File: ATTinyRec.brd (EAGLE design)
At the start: 15.7 x 29.3 mm, 10 parts, among them IC1 MAX631CPA, IC2 REG1117, M1 ELECTRET_MICROPHON-WM-62PC/62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, U1 ATTINY85-20SU, U2 USD-SOCKETUSD

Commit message: Debugging
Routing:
- net N$10: track 50.1 -> 69.5 mm, vias 0 -> 1
- net N$8: track 9.90 -> 0.00 mm, vias 1 -> 0
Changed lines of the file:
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@@
 <contactref element="M1" pad="1"/>
 <contactref element="R1" pad="2"/>
-<wire x1="14.1732" y1="25.8318" x2="13.716" y2="26.289" width="0.254" layer="1"/>
-<wire x1="16.2306" y1="25.8318" x2="14.1732" y2="25.8318" width="0.254" layer="1"/>
-<wire x1="17.3736" y1="24.6888" x2="16.2306" y2="25.8318" width="0.254" layer="1"/>
-<wire x1="17.3736" y1="24.6888" x2="17.46" y2="24.511" width="0.254" layer="1"/>
-<via x="16.2306" y="25.8318" extent="1-16" drill="0.6"/>
-<wire x1="16.2306" y1="25.8318" x2="18.685" y2="25.8318" width="0.4064" layer="16"/>
-<wire x1="18.685" y1="25.8318" x2="18.685" y2="28.763" width="0.4064" layer="16"/>
+<wire x1="17.46" y1="24.511" x2="18.685" y2="28.763" width="0" layer="19" extent="1-1"/>
 </signal>
 <signal name="N$9">
@@
 <wire x1="9.8298" y1="23.3172" x2="9.8298" y2="24.6888" width="0.254" layer="1"/>
 <wire x1="11.176" y1="21.971" x2="9.8298" y2="23.3172" width="0.254" layer="1"/>
-<wire x1="9.8298" y1="24.6888" x2="17.018" y2="27.1526" width="0" layer="19" extent="1-1"/>
-<wire x1="9.406" y1="24.257" x2="9.8298" y2="24.6888" width="0" layer="19" extent="1-1"/>
+<wire x1="17.018" y1="27.1526" x2="18.796" y2="27.1526" width="0.4064" layer="1"/>
+<wire x1="18.796" y1="27.1526" x2="18.796" y2="26.924" width="0.4064" layer="1"/>
+<via x="18.796" y="26.924" extent="1-16" drill="0.6" shape="square"/>
+<wire x1="18.796" y1="26.924" x2="18.796" y2="19.558" width="0.4064" layer="16"/>
+<wire x1="18.796" y1="19.558" x2="11.176" y2="19.558" width="0.4064" layer="16"/>
+<wire x1="11.176" y1="19.558" x2="11.176" y2="21.971" width="0.4064" layer="16"/>
+<wire x1="9.8298" y1="24.6888" x2="9.406" y2="24.257" width="0" layer="19" extent="1-1"/>
 </signal>
 <signal name="N$11">

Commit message: Component Replacements
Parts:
- removed IC1: MAX631CPA, maxim:DIL08
- removed IC2: REG1117, burr-brown:SOT223
- removed LED1: (no value), led:SMARTLED-TTW
- added C2: 10 µF, rcl:C0805K
- added D1: (no value), diode:DO214AC
- added JP1: AVR_SPI_PRG_6TESTPOINTS, SparkFun-Connectors:2X3_TEST_POINTS
- added R2: 976k, resistor:M0805
- added R3: 562k, resistor:M0805
- added U$1: MCP1640, GeekAmmo:SOT23-6
- C1: value 100 ÂµF -> 4.7 µF
- L1: value (none) -> 4.7 µH
- U1: value ATTINY85-20SU -> (none); device Atmel_By_element14_Batch_1-00:SOIC127P798X216-8N -> SparkFun-DigitalIC:MLF32-PAD
- moved M1 69.4 mm to (-47.0, 47.0)
- moved R1 66.3 mm to (-41.9, 55.9)
- moved C1 63.2 mm to (-48.3, 54.6), turned to 0 degrees
- moved U2 57.0 mm to (-21.6, 6.35), turned to 0 degrees
- moved L1 48.0 mm to (-24.1, 55.9), turned to 0 degrees
- moved U1 40.3 mm to (-16.5, 55.9), turned to 0 degrees
- moved G1 34.0 mm to (-27.9, 31.8), turned to 0 degrees
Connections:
- removed net N$11: C1.1, IC1.5, IC2.3
- new net N$20: JP1.5, U1.29
- new net NET': U1.18, U1.4, U1.6
- net N$1: now also C1.1, G1.+, L1.1, U$1.3, U$1.6; no longer U1.1
- net N$10: now also C2.1, D1.A, R2.2, U$1.5; no longer C1.2, G1.-, IC1.1, IC1.3, IC1.7, IC2.1, LED1.C@1, M1.2, U1.4, U2.6
- net N$13: now also U1.2, U2.2; no longer LED1.A@1
- net N$2: now also R2.1, R3.2, U$1.4; no longer IC2.2, R1.1, U1.8, U2.4
- net N$3: no longer IC1.4
- net N$4: now also C1.2, C2.2, G1.-, JP1.6, M1.2, R3.1, U$1.2, U1.21, U1.3, U1.5, U1.PAD, U2.6, U2.GND1, U2.GND2; no longer G1.+, L1.1
- net N$5: now also D1.C, JP1.2, R1.1, U1.20, U2.4; no longer U1.7, U2.5
- net N$6: now also JP1.4, U1.15; no longer U1.6
- net N$7: now also JP1.1, U1.16; no longer U1.5
- net N$8: now also U1.28
- net N$9: now also JP1.3, U1.17, U2.5; no longer U1.3, U2.2
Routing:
- net N$10: track 69.5 -> 0.00 mm, vias 1 -> 0
- net N$2: track 36.2 -> 0.00 mm, vias 2 -> 0
- net N$11: track 19.1 -> 0.00 mm
- net N$6: track 13.3 -> 0.00 mm, vias 2 -> 0
- net N$9: track 13.1 -> 0.00 mm
- net N$3: track 12.7 -> 0.00 mm
- net N$5: track 8.57 -> 0.00 mm
- net N$7: track 7.45 -> 0.00 mm
- net N$4: track 2.36 -> 0.00 mm
- net N$1: track 0.83 -> 0.00 mm
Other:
- board size 15.7 x 29.3 mm -> 100 x 80 mm

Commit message: Routed
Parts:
- removed JP1: AVR_SPI_PRG_6TESTPOINTS, SparkFun-Connectors:2X3_TEST_POINTS
- added U$2: AVR_MINI_PROGSMD, SparkFun-Connectors:AVR_MINI_PROG
- C1, C2: device rcl:C0805K -> rcl:C0402
- G1: value SL-150-1/2AA/PR -> SL-340/P; device battery:SL-150-1/2AA/PR -> battery:BEL/P
- L1: device rcl:L2825P -> resistor:L2012C
- R1: device resistor:M0805 -> rcl:R0402
- R2: value 976k -> 660k; device resistor:M0805 -> rcl:R0402
- R3: value 562k -> 309k; device resistor:M0805 -> rcl:R0402
- moved D1 73.2 mm to (5.84, 1.02), turned to 180 degrees
- moved M1 72.7 mm to (12.7, 5.46)
- moved C1 71.0 mm to (1.65, 4.06), turned to 90 degrees
- moved R1 70.9 mm to (6.86, 4.45)
- moved R3 64.8 mm to (5.08, 6.48)
- moved C2 58.9 mm to (1.65, 7.49), turned to 270 degrees
- moved U$1 55.6 mm to (2.54, 16.6), turned to 180 degrees
- moved R2 54.1 mm to (4.06, 14.2), turned to 270 degrees
- moved U1 54.0 mm to (5.97, 6.73), flipped to the bottom, turned to 180 degrees
- moved L1 47.8 mm to (3.56, 16.9), flipped to the bottom, turned to 270 degrees
- moved U2 41.3 mm to (7.62, 35.6), turned to 180 degrees
- moved G1 32.2 mm to (1.52, 18.7), turned to 90 degrees
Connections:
- removed net N$5: D1.C, JP1.2, R1.1, U1.20, U2.4
- net N$20: now also U$2.3; no longer JP1.5
- net N$3: now also U$1.1
- net N$4: now also U$2.2; no longer JP1.6
- net N$6: now also U$2.4; no longer JP1.4
- net N$7: now also U$2.6; no longer JP1.1
- net N$9: now also U$2.5; no longer JP1.3
- net NET': now also D1.C, R1.1, U$2.1, U1.20, U2.4
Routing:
- net N$4: track 0.00 -> 85.7 mm, vias 0 -> 3
- net NET': track 0.00 -> 46.7 mm, vias 0 -> 3
- net N$1: track 0.00 -> 26.6 mm, vias 0 -> 1
- net N$13: track 0.00 -> 21.5 mm, vias 0 -> 1
- net N$2: track 0.00 -> 19.7 mm, vias 0 -> 2
- net N$10: track 0.00 -> 19.1 mm
- net N$20: track 0.00 -> 19.0 mm
- net N$6: track 0.00 -> 18.8 mm, vias 0 -> 2
- net N$9: track 0.00 -> 15.3 mm, vias 0 -> 4
- net N$7: track 0.00 -> 14.2 mm
- net N$8: track 0.00 -> 11.2 mm, vias 0 -> 1
- net N$3: track 0.00 -> 1.85 mm
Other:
- board size 100 x 80 mm -> 14.9 x 20.3 mm

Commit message: Latest Updates
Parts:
- C1: value 4.7 µF -> 4.7 ÂµF
- C2: value 10 µF -> 10 ÂµF
- L1: value 4.7 µH -> 4.7 ÂµH
- moved R2 7.08 mm to (7.87, 8.26), turned to 180 degrees
- moved U$1 6.73 mm to (9.27, 16.6)
- moved U1 3.02 mm to (6.73, 9.65), turned to 0 degrees
- moved R3 2.81 mm to (7.87, 6.22)
- moved U2 2.09 mm to (9.65, 36.1), flipped to the bottom
- moved L1 1.94 mm to (3.17, 15.0), flipped to the top
- moved D1 1.02 mm to (5.97, 2.03)
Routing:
- net N$9: track 15.3 -> 43.5 mm
- net N$7: track 14.2 -> 26.0 mm, vias 0 -> 3
- net N$2: track 19.7 -> 8.10 mm, vias 2 -> 0
- net N$20: track 19.0 -> 7.55 mm, vias 0 -> 1
- net N$4: track 85.7 -> 96.6 mm, vias 3 -> 4
- net N$13: track 21.5 -> 10.7 mm, vias 1 -> 0
- net N$8: track 11.2 -> 19.5 mm, vias 1 -> 3
- net N$1: track 26.6 -> 33.8 mm, vias 1 -> 2
- net N$3: track 1.85 -> 7.50 mm
- net N$6: track 18.8 -> 22.1 mm, vias 2 -> 3
- net N$10: track 19.1 -> 21.7 mm
- net NET': track 46.7 -> 45.4 mm, vias 3 -> 4
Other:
- board size 14.9 x 20.3 mm -> 15.3 x 21.5 mm

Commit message: Board PDFs
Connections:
- new net S$6: U2.GND1
- net N$4: no longer U2.GND1, U2.GND2
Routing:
- net N$4: track 96.6 -> 67.2 mm
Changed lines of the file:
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@@
 <?xml version="1.0" encoding="utf-8"?>
 <!DOCTYPE eagle SYSTEM "eagle.dtd">
-<eagle version="7.2.0">
+<eagle version="6.5.0">
 <drawing>
 <settings>
@@
 <pass name="Default">
 <param name="RoutingGrid" value="1mil"/>
-<param name="AutoGrid" value="0"/>
-<param name="Efforts" value="0"/>
-<param name="TopRouterVariant" value="1"/>
 <param name="tpViaShape" value="octagon"/>
 <param name="PrefDir.1" value="*"/>
@@
 <via x="10.16" y="8.1788" extent="1-16" drill="0.6096" shape="octagon"/>
 </signal>
+<signal name="S$6">
+<contactref element="U2" pad="GND1"/>
+<wire x1="3.3782" y1="34.5948" x2="3.377" y2="34.593" width="0.254" layer="16"/>
+</signal>
+<signal name="S$4">
+</signal>
 <signal name="N$4">
 <contactref element="G1" pad="-"/>
@@
 <contactref element="C1" pad="2"/>
 <contactref element="U2" pad="6"/>
-<contactref element="U2" pad="GND1"/>
-<contactref element="U2" pad="GND2"/>
 <contactref element="U1" pad="PAD"/>
 <contactref element="U1" pad="5"/>
@@
 <via x="2.286" y="5.7912" extent="1-16" drill="0.6096" shape="octagon"/>
 <via x="12.3444" y="9.4488" extent="1-16" drill="0.6096" shape="octagon"/>
-<wire x1="16.0274" y1="34.5948" x2="7.239" y2="34.5948" width="0.254" layer="16"/>
-<wire x1="7.239" y1="34.5948" x2="3.3782" y2="34.5948" width="0.254" layer="16"/>
-<wire x1="17.018" y1="35.5854" x2="16.0274" y2="34.5948" width="0.254" layer="16"/>
-<wire x1="3.3782" y1="34.5948" x2="3.377" y2="34.593" width="0.254" layer="16"/>
-<wire x1="17.018" y1="35.5854" x2="17.027" y2="35.593" width="0.254" layer="16"/>
-<wire x1="7.352" y1="19.268" x2="7.352" y2="34.4818" width="0.2032" layer="16"/>
-<wire x1="7.352" y1="34.4818" x2="7.239" y2="34.5948" width="0.2032" layer="16"/>
 </signal>
 <signal name="N$2">
@@
 <contactref element="R2" pad="2"/>
 <contactref element="D1" pad="A"/>
-<wire x1="4.5974" y1="3.7846" x2="1.651" y2="8.128" width="0.254" layer="1"/>
-<wire x1="4.5974" y1="2.6924" x2="4.5974" y2="3.7846" width="0.254" layer="1"/>
-<wire x1="4.5974" y1="4.6736" x2="4.5974" y2="3.7846" width="0.254" layer="1"/>
+<wire x1="4.5974" y1="2.6924" x2="4.5974" y2="4.6736" width="0.254" layer="1"/>
+<wire x1="4.5974" y1="4.6736" x2="4.5974" y2="3.7846" width="0" layer="19" extent="1-16"/>
 <wire x1="3.937" y1="2.032" x2="4.5974" y2="2.6924" width="0.254" layer="1"/>
 <wire x1="1.651" y1="8.128" x2="1.651" y2="8.143" width="0.254" layer="1"/>
@@
 <wire x1="8.3058" y1="13.843" x2="8.321" y2="13.837" width="0.254" layer="1"/>
 <wire x1="7.1374" y1="8.3566" x2="7.224" y2="8.255" width="0.254" layer="1"/>
+<wire x1="1.651" y1="8.128" x2="1.778" y2="8.128" width="0.254" layer="1"/>
+<wire x1="1.778" y1="8.128" x2="2.54" y2="7.366" width="0.254" layer="1"/>
+<wire x1="2.54" y1="7.366" x2="2.54" y2="6.604" width="0.254" layer="1"/>
+<wire x1="2.54" y1="6.604" x2="3.302" y2="5.842" width="0.254" layer="1"/>
+<wire x1="3.302" y1="5.842" x2="3.302" y2="5.08" width="0.254" layer="1"/>
+<wire x1="3.302" y1="5.08" x2="3.683" y2="4.699" width="0.254" layer="1"/>
+<wire x1="3.683" y1="4.699" x2="4.572" y2="4.699" width="0.254" layer="1"/>
+<wire x1="4.572" y1="4.699" x2="4.5974" y2="4.6736" width="0.254" layer="1"/>
 </signal>
 <signal name="N$3">

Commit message: remade board and schematic consistent
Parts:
- C1: value 4.7 ÂµF -> 4.7 µF
- C2: value 10 ÂµF -> 10 µF
- L1: value 4.7 ÂµH -> 4.7 µH
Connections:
- removed net S$6: U2.GND1
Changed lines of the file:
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@@
 <?xml version="1.0" encoding="utf-8"?>
 <!DOCTYPE eagle SYSTEM "eagle.dtd">
-<eagle version="6.5.0">
+<eagle version="6.6.0">
 <drawing>
 <settings>
@@
 </autorouter>
 <elements>
-<element name="C1" library="rcl" package="C0402" value="4.7 ÂµF" x="1.651" y="4.064" rot="R90"/>
-<element name="C2" library="rcl" package="C0402" value="10 ÂµF" x="1.651" y="7.493" rot="R270"/>
+<element name="C1" library="rcl" package="C0402" value="4.7 µF" x="1.651" y="4.064" rot="R90"/>
+<element name="C2" library="rcl" package="C0402" value="10 µF" x="1.651" y="7.493" rot="R270"/>
 <element name="D1" library="diode" package="DO214AC" value="" x="5.969" y="2.032" rot="R180"/>
 <element name="G1" library="battery" package="BEL/P" value="SL-340/P" x="1.524" y="18.669" rot="R90"/>
-<element name="L1" library="resistor" package="L2012C" value="4.7 ÂµH" x="3.175" y="14.986" rot="R270"/>
+<element name="L1" library="resistor" package="L2012C" value="4.7 µH" x="3.175" y="14.986" rot="R270"/>
 <element name="M1" library="microphon" package="WM-62PC/62PK" value="ELECTRET_MICROPHON-WM-62PC/62PK" x="12.7" y="5.461"/>
 <element name="R1" library="rcl" package="R0402" value="2k2" x="6.858" y="4.445"/>
@@
 <via x="10.16" y="8.1788" extent="1-16" drill="0.6096" shape="octagon"/>
 </signal>
-<signal name="S$6">
-<contactref element="U2" pad="GND1"/>
-<wire x1="3.3782" y1="34.5948" x2="3.377" y2="34.593" width="0.254" layer="16"/>
-</signal>
 <signal name="S$4">

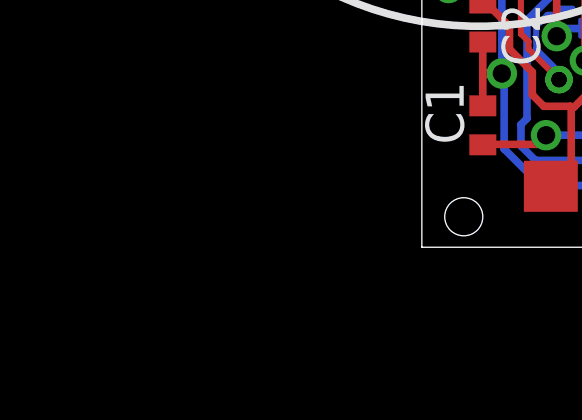
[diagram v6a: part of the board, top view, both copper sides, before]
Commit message: added pullup resistor
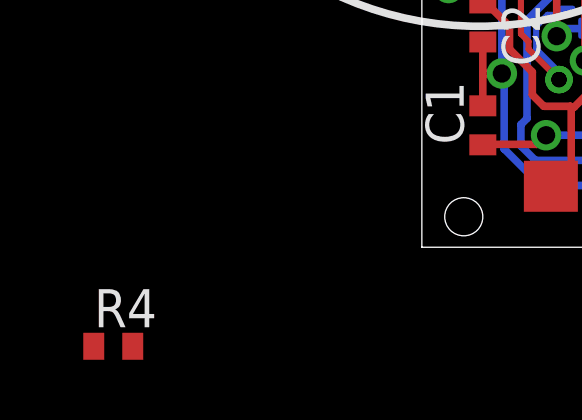
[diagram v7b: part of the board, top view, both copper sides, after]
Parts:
- added R4: 10k, rcl:R0402
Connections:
- net N$4 renamed GND
- net N$6 renamed MOSI
- net N$7 renamed MISO
- net N$9 renamed SCK
- removed net N$20: U$2.3, U1.29
- removed net NET': D1.C, R1.1, U$2.1, U1.18, U1.20, U1.4, U1.6, U2.4
- new net RESET: R4.1, U$2.3, U1.29
- new net VCC: D1.C, R1.1, R4.2, U$2.1, U1.18, U1.20, U1.4, U1.6, U2.4
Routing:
- net VCC: track 0.00 -> 45.4 mm, vias 0 -> 4
- net NET': track 45.4 -> 0.00 mm, vias 4 -> 0
- net RESET: track 0.00 -> 7.55 mm, vias 0 -> 1
- net N$20: track 7.55 -> 0.00 mm, vias 1 -> 0
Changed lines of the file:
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@@
 <element name="U2" library="SparkFun-Connectors" package="USD-SOCKET-PP" value="USD-SOCKETUSD" x="9.652" y="36.068" rot="MR180"/>
 <element name="U$2" library="SparkFun-Connectors" package="AVR_MINI_PROG" value="AVR_MINI_PROGSMD" x="13.716" y="9.652" rot="R90"/>
+<element name="R4" library="rcl" package="R0402" value="10k" x="-10.668" y="-3.302"/>
 </elements>
 <signals>
@@
 <via x="8.5852" y="4.2164" extent="1-16" drill="0.6096" shape="octagon"/>
 </signal>
-<signal name="N$6">
+<signal name="MOSI">
 <contactref element="U1" pad="15"/>
 <contactref element="U2" pad="3"/>
@@
 <via x="11.4046" y="15.4686" extent="1-16" drill="0.6096" shape="octagon"/>
 </signal>
-<signal name="N$7">
+<signal name="MISO">
 <contactref element="U2" pad="7"/>
 <contactref element="U1" pad="16"/>
@@
 <via x="4.953" y="17.8054" extent="1-16" drill="0.6096" shape="octagon"/>
 </signal>
-<signal name="N$9">
+<signal name="SCK">
 <contactref element="U2" pad="5"/>
 <contactref element="U1" pad="17"/>
@@
 <wire x1="11.7602" y1="19.2532" x2="11.752" y2="19.268" width="0.254" layer="16"/>
 </signal>
-<signal name="NET'">
+<signal name="VCC">
 <contactref element="U1" pad="6"/>
 <contactref element="U1" pad="4"/>
@@
 <via x="3.937" y="12.4206" extent="1-16" drill="0.6096" shape="octagon"/>
 <via x="10.541" y="2.0828" extent="1-16" drill="0.6096" shape="octagon"/>
-</signal>
-<signal name="N$20">
+<contactref element="R4" pad="2"/>
+<wire x1="2.921" y1="3.3782" x2="-10.018" y2="-3.302" width="0" layer="19" extent="1-16"/>
+</signal>
+<signal name="RESET">
 <contactref element="U1" pad="29"/>
 <contactref element="U$2" pad="3"/>
@@
 <wire x1="13.716" y1="12.6746" x2="13.716" y2="12.652" width="0.254" layer="1"/>
 <via x="11.2776" y="12.9794" extent="1-16" drill="0.6096" shape="octagon"/>
+<contactref element="R4" pad="1"/>
+<wire x1="-11.318" y1="-3.302" x2="6.981" y2="12.002" width="0" layer="19" extent="1-16"/>
 </signal>
 <signal name="N$1">
@@
 <signal name="S$4">
 </signal>
-<signal name="N$4">
+<signal name="GND">
 <contactref element="G1" pad="-"/>
 <contactref element="U$1" pad="2"/>
@@
 <contactref element="D1" pad="A"/>
 <wire x1="4.5974" y1="2.6924" x2="4.5974" y2="4.6736" width="0.254" layer="1"/>
-<wire x1="4.5974" y1="4.6736" x2="4.5974" y2="3.7846" width="0" layer="19" extent="1-16"/>
 <wire x1="3.937" y1="2.032" x2="4.5974" y2="2.6924" width="0.254" layer="1"/>
 <wire x1="1.651" y1="8.128" x2="1.651" y2="8.143" width="0.254" layer="1"/>

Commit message: Fixed Board Layout
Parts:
- moved R4 26.5 mm to (11.6, 11.0), turned to 270 degrees
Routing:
- net SCK: track 43.5 -> 38.6 mm
- net VCC: track 45.4 -> 50.0 mm
- net RESET: track 7.55 -> 9.11 mm
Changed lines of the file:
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@@
 <?xml version="1.0" encoding="utf-8"?>
 <!DOCTYPE eagle SYSTEM "eagle.dtd">
-<eagle version="6.6.0">
+<eagle version="7.1.0">
 <drawing>
 <settings>
@@
 <pass name="Default">
 <param name="RoutingGrid" value="1mil"/>
+<param name="AutoGrid" value="1"/>
+<param name="Efforts" value="0"/>
+<param name="TopRouterVariant" value="1"/>
 <param name="tpViaShape" value="octagon"/>
 <param name="PrefDir.1" value="*"/>
@@
 <element name="U2" library="SparkFun-Connectors" package="USD-SOCKET-PP" value="USD-SOCKETUSD" x="9.652" y="36.068" rot="MR180"/>
 <element name="U$2" library="SparkFun-Connectors" package="AVR_MINI_PROG" value="AVR_MINI_PROGSMD" x="13.716" y="9.652" rot="R90"/>
-<element name="R4" library="rcl" package="R0402" value="10k" x="-10.668" y="-3.302"/>
+<element name="R4" library="rcl" package="R0402" value="10k" x="11.557" y="11.049" rot="R270"/>
 </elements>
 <signals>
@@
 <wire x1="10.6172" y1="12.446" x2="10.287" y2="12.7762" width="0.254" layer="1"/>
 <wire x1="10.6172" y1="9.4488" x2="10.6172" y2="12.446" width="0.254" layer="1"/>
-<wire x1="11.2268" y1="8.8392" x2="10.6172" y2="9.4488" width="0.254" layer="1"/>
-<wire x1="11.8872" y1="8.1788" x2="11.2268" y2="8.8392" width="0.254" layer="16"/>
+<wire x1="11.3538" y1="8.2042" x2="10.6172" y2="9.4488" width="0.254" layer="1"/>
+<wire x1="11.8872" y1="8.1788" x2="11.3538" y2="8.2042" width="0.254" layer="16"/>
 <wire x1="11.8872" y1="6.604" x2="11.8872" y2="8.1788" width="0.254" layer="16"/>
 <wire x1="11.7094" y1="6.4262" x2="11.8872" y2="6.604" width="0.254" layer="16"/>
@@
 <wire x1="11.6078" y1="6.3246" x2="11.7" y2="6.411" width="0.254" layer="16"/>
 <via x="10.287" y="14.351" extent="1-16" drill="0.6096" shape="octagon"/>
-<via x="11.2268" y="8.8392" extent="1-16" drill="0.6096" shape="octagon"/>
+<via x="11.3538" y="8.2042" extent="1-16" drill="0.6096" shape="octagon"/>
 <via x="8.5852" y="4.2164" extent="1-16" drill="0.6096" shape="octagon"/>
 </signal>
@@
 <wire x1="4.5212" y1="16.8148" x2="3.556" y2="17.78" width="0.2032" layer="1"/>
 <via x="3.556" y="17.78" extent="1-16" drill="0.6"/>
-<wire x1="3.556" y1="17.78" x2="3.048" y2="18.288" width="0.2032" layer="16"/>
-<wire x1="3.048" y1="18.288" x2="3.048" y2="19.685" width="0.2032" layer="16"/>
-<wire x1="3.048" y1="19.685" x2="2.159" y2="20.574" width="0.2032" layer="16"/>
-<wire x1="2.159" y1="20.574" x2="0.762" y2="20.574" width="0.2032" layer="16"/>
-<wire x1="0.762" y1="20.574" x2="0" y2="19.812" width="0.2032" layer="16"/>
-<wire x1="0" y1="19.812" x2="0" y2="9.144" width="0.2032" layer="16"/>
+<wire x1="3.556" y1="17.78" x2="3.048" y2="17.78" width="0.2032" layer="16"/>
+<wire x1="3.048" y1="17.78" x2="2.794" y2="17.399" width="0.2032" layer="16"/>
+<wire x1="2.794" y1="17.399" x2="2.667" y2="17.145" width="0.2032" layer="16"/>
+<wire x1="2.667" y1="17.145" x2="0.635" y2="17.145" width="0.2032" layer="16"/>
+<wire x1="0.635" y1="17.145" x2="0" y2="16.637" width="0.2032" layer="16"/>
+<wire x1="0" y1="16.637" x2="0" y2="9.144" width="0.2032" layer="16"/>
 <wire x1="0" y1="9.144" x2="0.508" y2="8.636" width="0.2032" layer="16"/>
 <via x="0.508" y="8.636" extent="1-16" drill="0.508" diameter="0.254"/>
@@
 <via x="10.541" y="2.0828" extent="1-16" drill="0.6096" shape="octagon"/>
 <contactref element="R4" pad="2"/>
-<wire x1="2.921" y1="3.3782" x2="-10.018" y2="-3.302" width="0" layer="19" extent="1-16"/>
+<wire x1="11.557" y1="10.399" x2="11.557" y2="9.144" width="0.254" layer="1"/>
+<wire x1="11.557" y1="9.144" x2="12.446" y2="8.255" width="0.254" layer="1"/>
+<wire x1="12.446" y1="8.255" x2="12.7508" y2="8.255" width="0.254" layer="1"/>
+<wire x1="12.7508" y1="8.255" x2="13.6398" y2="9.144" width="0.254" layer="1"/>
+<wire x1="13.6398" y1="9.144" x2="13.6398" y2="9.5758" width="0.254" layer="1"/>
+<wire x1="13.6398" y1="9.5758" x2="13.716" y2="9.652" width="0.254" layer="1"/>
 </signal>
 <signal name="RESET">
@@
 <via x="11.2776" y="12.9794" extent="1-16" drill="0.6096" shape="octagon"/>
 <contactref element="R4" pad="1"/>
-<wire x1="-11.318" y1="-3.302" x2="6.981" y2="12.002" width="0" layer="19" extent="1-16"/>
+<wire x1="11.2776" y1="12.9794" x2="11.557" y2="12.9794" width="0.4064" layer="1"/>
+<wire x1="11.557" y1="12.9794" x2="11.557" y2="11.699" width="0.4064" layer="1"/>
 </signal>
 <signal name="N$1">
@@
 <via x="3.556" y="17.78" extent="1-16" drill="0.6"/>
 </signal>
-<signal name="S$2">
-<via x="1.016" y="16.383" extent="1-16" drill="0.6"/>
-</signal>
 <signal name="S$3">
